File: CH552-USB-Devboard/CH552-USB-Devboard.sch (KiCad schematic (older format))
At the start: 26 parts, among them J1 Conn_01x11_Male, J2 Conn_01x11_Male, J3 USB_C_Receptacle, Q1 CPH6337, SW1 SW_Push, SW2 SW_Push, U1 CH552T, U2 CH552G, U3 MIC5504-3.3YM5, Y1 Crystal

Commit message: add resistors for BOOTL and CC lines, remove LDO
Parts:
- removed C5, C6: 100uF, Capacitor_SMD:C_0603_1608Metric_Pad1.05x0.95mm_HandSolder, symbol Device:C_Small
- removed D4: SMCJ17A+, Diode_SMD:D_1812_4532Metric, symbol Device:D_ALT
- removed JP2: Jumper, Jumper:SolderJumper-2_P1.3mm_Bridged_RoundedPad1.0x1.5mm, symbol Device:Jumper
- removed Q1: CPH6337, TO_SOT_Packages_SMD:SOT-23-6, symbol OnSemi:CPH6337
- removed U3: MIC5504-3.3YM5, Package_TO_SOT_SMD:SOT-23-5, symbol Regulator_Linear:MIC5504-3.3YM5
- removed Y1: Crystal, Crystal:Crystal_SMD_HC49-SD, symbol Device:Crystal
- added D4, D5: e.g. 1N4148, C917006, C708767, Diode_SMD:D_SOD-523, symbol Device:D
- added R1, R2: 68, Resistor_SMD:R_0603_1608Metric_Pad0.98x0.95mm_HandSolder, symbol Device:R_Small
- added R6: 22k, Resistor_SMD:R_0603_1608Metric_Pad0.98x0.95mm_HandSolder, symbol Device:R_Small
- added R7: 220, Resistor_SMD:R_0603_1608Metric_Pad0.98x0.95mm_HandSolder, symbol Device:R_Small
- C3: value 100uF -> 100nF
- C4, C7: value 1uF -> DNP/1uF
- J3: symbol Connector:USB_C_Receptacle -> CH552-USB-Devboard-rescue:USB_C_Receptacle-Connector
- R3, R4: value 330r -> 1k; footprint Resistor_SMD:R_0603_1608Metric_Pad1.05x0.95mm_HandSolder -> Resistor_SMD:R_0603_1608Metric_Pad0.98x0.95mm_HandSolder
- R5: value 300r -> 1k; footprint Resistor_SMD:R_0603_1608Metric_Pad1.05x0.95mm_HandSolder -> Resistor_SMD:R_0603_1608Metric_Pad0.98x0.95mm_HandSolder
- U1: symbol MCU_WCH:CH552T -> CH552-USB-Devboard-rescue:CH552T-MCU_WCH
- U2: symbol MCU_WCH:CH552G -> CH552-USB-Devboard-rescue:CH552G-MCU_WCH
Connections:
- wire segments 161 -> 151
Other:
- note added: "FIXME:\n- BOOTL switch needs 22k resistor\n- RST switch is quite useless (BOOTL needs POR, I think)\n- LDO is not necessary (integrated into the CH552)\n- add solder jumper to bridge Q1\n- add SOT-23 alternative for Q1\n- move crystal to top side?\n- C3 should be 100nF\n- C5/C6 should be *much* smaller, e.g. 12 pF"
- note removed: "Prevents Reverse powering of VBUS"
- note removed: "Reverse Protection\n"
- moved on the sheet: C4

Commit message: add reference voltage for ACMP, replace symbol for USB connector
That symbol was causing warnings because some of the pins are not
available on the footprint. Kicad has the appropriate symbol so
let's use that.
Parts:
- added JP2: Jumper, Jumper:SolderJumper-2_P1.3mm_Bridged_RoundedPad1.0x1.5mm, symbol Jumper:SolderJumper_2_Bridged
- added JP3: Jumper, Jumper:SolderJumper-2_P1.3mm_Open_RoundedPad1.0x1.5mm, symbol Jumper:SolderJumper_2_Open
- added R8: 1k, Resistor_SMD:R_0603_1608Metric_Pad0.98x0.95mm_HandSolder, symbol Device:R_Small
- added R9: 10k, Resistor_SMD:R_0603_1608Metric_Pad0.98x0.95mm_HandSolder, symbol Device:R_Small
- J3: symbol CH552-USB-Devboard-rescue:USB_C_Receptacle-Connector -> Connector:USB_C_Receptacle_USB2.0
- JP1: symbol Device:Jumper -> Jumper:SolderJumper_2_Bridged
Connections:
- net +3V3: now also R9.2
- net GND: now also R8.2
- net P3.2: now also JP2.2 (B), R8.1, R9.1
- net P3.3: now also JP3.2 (B); no longer R7.1
- new net: JP2.1 (A), JP3.1 (A), R7.1
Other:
- note added: "0.5V ref. voltage for ACMP\nOptions:\n1. Both resistors external\n2. Use 10k VBUS pulldown plus ext. PU\n3. Use int. PU plus ext. PD (high variation)\n4. Use int. PU and PD (high variation, 0.5V)"
- note added: "I think P3.2 can do double duty\nbecause we only need the reference\nduring RX and the diode should\nensure that CC1/2 doesn't influence\nthe reference (if Vf>0.5V)."
- note removed: "FIXME:\n- BOOTL switch needs 22k resistor\n- RST switch is quite useless (BOOTL needs POR, I think)\n- LDO is not necessary (integrated into the CH552)\n- add solder jumper to bridge Q1\n- add SOT-23 alternative for Q1\n- move crystal to top side?\n- C3 should be 100nF\n- C5/C6 should be *much* smaller, e.g. 12 pF"
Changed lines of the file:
@@
-	1    0    0    -1
-$EndComp
-$Comp
-L CH552-USB-Devboard-rescue:USB_C_Receptacle-Connector J3
-U 1 1 5F0EEE62
-P 5650 2150
-F 0 "J3" H 5755 3717 50  0000 C CNN
-F 1 "USB_C_Receptacle" H 5755 3626 50  0000 C CNN
-F 2 "footprint:VACON_CSP_USC16_TR" H 5800 2150 50  0001 C CNN
-F 3 "http://www.usb.org/developers/docs/usb_31_033017.zip" H 5800 2150 50  0001 C CNN
-	1    5650 2150
 	1    0    0    -1
 $EndComp
@@
 	6500 1750 6950 1750
 Wire Wire Line
-	5350 3750 5350 4100
-Wire Wire Line
-	5350 4100 5450 4100
-Wire Wire Line
-	5750 3750 5750 4100
-Wire Wire Line
-	5650 3750 5650 4100
-Connection ~ 5650 4100
-Wire Wire Line
-	5650 4100 5750 4100
-Wire Wire Line
-	5550 3750 5550 4100
-Connection ~ 5550 4100
-Wire Wire Line
-	5550 4100 5650 4100
-Wire Wire Line
-	5450 3750 5450 4100
-Connection ~ 5450 4100
-Wire Wire Line
-	5450 4100 5550 4100
-Wire Wire Line
-	5750 4100 5750 4350
-Connection ~ 5750 4100
-$Comp
-L power:GND #PWR0103
-U 1 1 5F12C15E
-P 5750 4350
-F 0 "#PWR0103" H 5750 4100 50  0001 C CNN
-F 1 "GND" H 5755 4177 50  0000 C CNN
-F 2 "" H 5750 4350 50  0001 C CNN
-F 3 "" H 5750 4350 50  0001 C CNN
-	1    5750 4350
-	1    0    0    -1
-$EndComp
-Wire Wire Line
-	6250 850  6750 850
-Wire Wire Line
-	6750 850  6750 700
-Wire Wire Line
-	6250 1150 6750 1150
-Wire Wire Line
-	6750 1150 6750 1050
-Connection ~ 6750 850
-Wire Wire Line
-	6250 1050 6750 1050
-Connection ~ 6750 1050
-Wire Wire Line
-	6750 1050 6750 950
-Wire Wire Line
-	6250 950  6750 950
-Connection ~ 6750 950
-Wire Wire Line
-	6750 950  6750 850
+	6250 1150 6350 1150
 $Comp
 L power:VBUS #PWR0104
 U 1 1 5F1419FC
-P 6750 700
-F 0 "#PWR0104" H 6750 550 50  0001 C CNN
-F 1 "VBUS" H 6765 873 50  0000 C CNN
-F 2 "" H 6750 700 50  0001 C CNN
-F 3 "" H 6750 700 50  0001 C CNN
-	1    6750 700
+P 6350 1050
+F 0 "#PWR0104" H 6350 900 50  0001 C CNN
+F 1 "VBUS" H 6365 1223 50  0000 C CNN
+F 2 "" H 6350 1050 50  0001 C CNN
+F 3 "" H 6350 1050 50  0001 C CNN
+	1    6350 1050
 	1    0    0    -1
 $EndComp
@@
 	1    0    0    -1
 $EndComp
-Text Notes 1250 -650 0    50   ~ 0
-FIXME:\n- BOOTL switch needs 22k resistor\n- RST switch is quite useless (BOOTL needs POR, I think)\n- LDO is not necessary (integrated into the CH552)\n- add solder jumper to bridge Q1\n- add SOT-23 alternative for Q1\n- move crystal to top side?\n- C3 should be 100nF\n- C5/C6 should be *much* smaller, e.g. 12 pF
-$Comp
-L Device:Jumper JP1
+$Comp
+L Jumper:SolderJumper_2_Bridged JP1
 U 1 1 60A07638
 P 8250 1850
 F 0 "JP1" H 8250 2114 50  0000 C CNN
-F 1 "Jumper" H 8250 2023 50  0000 C CNN
+F 1 "Jumper" H 8250 2023 50  0001 C CNN
 F 2 "Jumper:SolderJumper-2_P1.3mm_Bridged_RoundedPad1.0x1.5mm" H 8250 1850 50  0001 C CNN
 F 3 "~" H 8250 1850 50  0001 C CNN
@@
 	1    0    0    -1
 $EndComp
-Wire Wire Line
-	7950 1850 7500 1850
-Wire Wire Line
-	8550 1850 9000 1850
 Wire Wire Line
 	9100 2300 9100 2550
@@
 Wire Wire Line
 	2500 2450 2850 2450
-Text Label 2850 2450 2    50   ~ 0
+Text Label 3650 2700 2    50   ~ 0
 P3.3
 Text Label 800  2300 0    50   ~ 0
@@
 Wire Wire Line
 	9100 4500 9700 4500
+Text Label 2850 2950 2    50   ~ 0
+P3.2
+$Comp
+L Device:R_Small R8
+U 1 1 60A0EBE8
+P 2400 2950
+F 0 "R8" V 2204 2950 50  0000 C CNN
+F 1 "1k" V 2295 2950 50  0000 C CNN
+F 2 "Resistor_SMD:R_0603_1608Metric_Pad0.98x0.95mm_HandSolder" H 2400 2950 50  0001 C CNN
+F 3 "~" H 2400 2950 50  0001 C CNN
+	1    2400 2950
+	0    1    1    0
+$EndComp
+Wire Wire Line
+	2850 2950 2600 2950
+$Comp
+L Device:R_Small R9
+U 1 1 60A17F33
+P 2400 3250
+F 0 "R9" V 2204 3250 50  0000 C CNN
+F 1 "10k" V 2295 3250 50  0000 C CNN
+F 2 "Resistor_SMD:R_0603_1608Metric_Pad0.98x0.95mm_HandSolder" H 2400 3250 50  0001 C CNN
+F 3 "~" H 2400 3250 50  0001 C CNN
+	1    2400 3250
+	0    1    1    0
+$EndComp
+Wire Wire Line
+	2500 3250 2600 3250
+Wire Wire Line
+	2600 3250 2600 2950
+Connection ~ 2600 2950
+Wire Wire Line
+	2600 2950 2500 2950
+$Comp
+L power:+3V3 #PWR0113
+U 1 1 60A21FA3
+P 2200 3250
+F 0 "#PWR0113" H 2200 3100 50  0001 C CNN
+F 1 "+3V3" H 2215 3423 50  0000 C CNN
+F 2 "" H 2200 3250 50  0001 C CNN
+F 3 "" H 2200 3250 50  0001 C CNN
+	1    2200 3250
+	0    -1   -1   0
+$EndComp
+Wire Wire Line
+	2200 3250 2300 3250
+$Comp
+L power:GND #PWR0115
+U 1 1 60A2BA53
+P 2200 2950
+F 0 "#PWR0115" H 2200 2700 50  0001 C CNN
+F 1 "GND" H 2205 2777 50  0000 C CNN
+F 2 "" H 2200 2950 50  0001 C CNN
+F 3 "" H 2200 2950 50  0001 C CNN
+	1    2200 2950
+	0    1    1    0
+$EndComp
+Wire Wire Line
+	2200 2950 2300 2950
+Text Notes 700  3600 0    50   ~ 0
+0.5V ref. voltage for ACMP\nOptions:\n1. Both resistors external\n2. Use 10k VBUS pulldown plus ext. PU\n3. Use int. PU plus ext. PD (high variation)\n4. Use int. PU and PD (high variation, 0.5V)
+$Comp
+L Jumper:SolderJumper_2_Bridged JP2
+U 1 1 60A4E06D
+P 3200 2450
+F 0 "JP2" H 3200 2600 50  0000 C CNN
+F 1 "Jumper" H 3200 2623 50  0001 C CNN
+F 2 "Jumper:SolderJumper-2_P1.3mm_Bridged_RoundedPad1.0x1.5mm" H 3200 2450 50  0001 C CNN
+F 3 "~" H 3200 2450 50  0001 C CNN
+	1    3200 2450
+	1    0    0    -1
+$EndComp
+$Comp
+L Jumper:SolderJumper_2_Open JP3
+U 1 1 60A50BC6
+P 3200 2700
+F 0 "JP3" H 3200 2800 50  0000 C CNN
+F 1 "Jumper" H 3200 2873 50  0001 C CNN
+F 2 "Jumper:SolderJumper-2_P1.3mm_Open_RoundedPad1.0x1.5mm" H 3200 2700 50  0001 C CNN
+F 3 "~" H 3200 2700 50  0001 C CNN
+	1    3200 2700
+	1    0    0    -1
+$EndComp
+Wire Wire Line
+	7500 1850 8100 1850
+Wire Wire Line
+	8400 1850 9000 1850
+Wire Wire Line
+	3650 2700 3350 2700
+Wire Wire Line
+	3050 2700 2850 2700
+Wire Wire Line
+	2850 2700 2850 2450
+Wire Wire Line
+	2850 2450 3050 2450
+Connection ~ 2850 2450
+Text Label 3650 2450 2    50   ~ 0
+P3.2
+Wire Wire Line
+	3650 2450 3350 2450
+Text Notes 2550 2250 0    50   ~ 0
+I think P3.2 can do double duty\nbecause we only need the reference\nduring RX and the diode should\nensure that CC1/2 doesn't influence\nthe reference (if Vf>0.5V).
+$Comp
+L power:GND #PWR0103
+U 1 1 5F12C15E
+P 5650 3250
+F 0 "#PWR0103" H 5650 3000 50  0001 C CNN
+F 1 "GND" H 5655 3077 50  0000 C CNN
+F 2 "" H 5650 3250 50  0001 C CNN
+F 3 "" H 5650 3250 50  0001 C CNN
+	1    5650 3250
+	1    0    0    -1
+$EndComp
+Connection ~ 5650 3000
+Wire Wire Line
+	5650 3000 5650 3250
+Wire Wire Line
+	5350 2650 5350 3000
+Wire Wire Line
+	5650 2650 5650 3000
+$Comp
+L Connector:USB_C_Receptacle_USB2.0 J3
+U 1 1 5F0EEE62
+P 5650 1750
+F 0 "J3" H 5755 3317 50  0000 C CNN
+F 1 "USB_C_Receptacle" H 5755 3226 50  0000 C CNN
+F 2 "footprint:VACON_CSP_USC16_TR" H 5800 1750 50  0001 C CNN
+F 3 "http://www.usb.org/developers/docs/usb_31_033017.zip" H 5800 1750 50  0001 C CNN
+	1    5650 1750
+	1    0    0    -1
+$EndComp
+Wire Wire Line
+	5350 3000 5650 3000
+Wire Wire Line
+	6350 1050 6350 1150
 $EndSCHEMATC

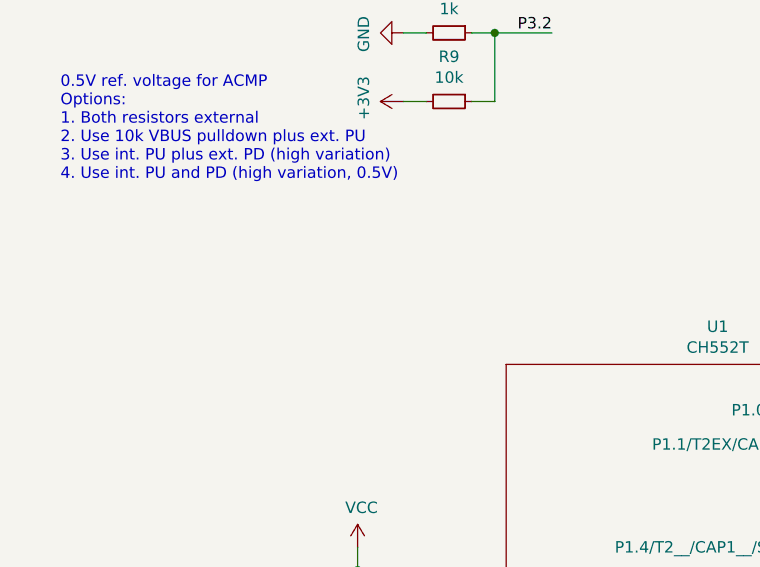
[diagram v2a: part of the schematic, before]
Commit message: add voltage divider for VBUS, optimize GND plane
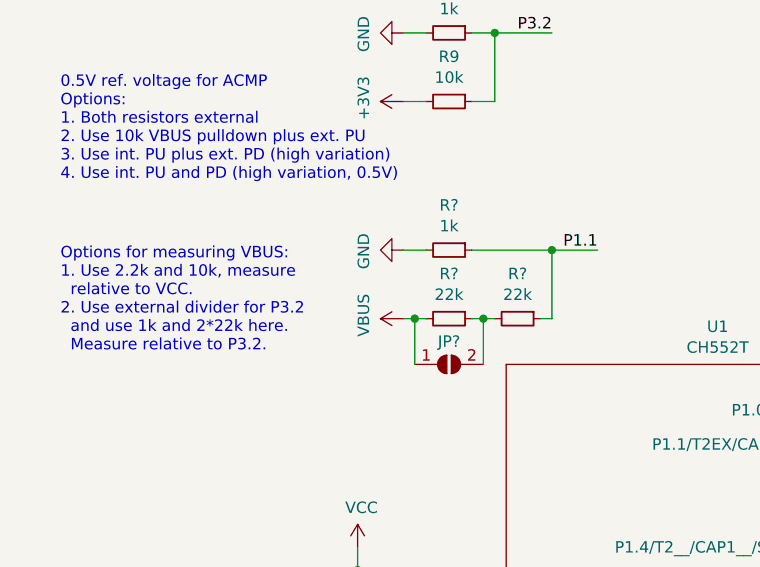
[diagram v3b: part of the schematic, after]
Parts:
- added JP?: Jumper, Jumper:SolderJumper-2_P1.3mm_Open_RoundedPad1.0x1.5mm, symbol Jumper:SolderJumper_2_Open
- added R?: 1k, Resistor_SMD:R_0603_1608Metric_Pad0.98x0.95mm_HandSolder, symbol Device:R_Small
- added R? (x2): 22k, Resistor_SMD:R_0603_1608Metric_Pad0.98x0.95mm_HandSolder, symbol Device:R_Small
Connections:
- net GND: now also R?.2
- net P1.1: now also R?.1, R?.1
- net VBUS: now also JP?.1 (A), R?.2
- new net: JP?.2 (B), R?.1, R?.2
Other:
- note added: "Options for measuring VBUS:\n1. Use 2.2k and 10k, measure\n relative to VCC.\n2. Use external divider for P3.2\n and use 1k and 2*22k here.\n Measure relative to P3.2."
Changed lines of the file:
@@
 Wire Wire Line
 	6350 1050 6350 1150
+Wire Wire Line
+	2850 3900 3050 3900
+Text Label 3050 3900 2    50   ~ 0
+P1.1
+$Comp
+L Device:R_Small R?
+U 1 1 60B6EE8A
+P 2400 3900
+F 0 "R?" V 2204 3900 50  0000 C CNN
+F 1 "1k" V 2295 3900 50  0000 C CNN
+F 2 "Resistor_SMD:R_0603_1608Metric_Pad0.98x0.95mm_HandSolder" H 2400 3900 50  0001 C CNN
+F 3 "~" H 2400 3900 50  0001 C CNN
+	1    2400 3900
+	0    1    1    0
+$EndComp
+$Comp
+L Device:R_Small R?
+U 1 1 60B79ACF
+P 2400 4200
+F 0 "R?" V 2204 4200 50  0000 C CNN
+F 1 "22k" V 2295 4200 50  0000 C CNN
+F 2 "Resistor_SMD:R_0603_1608Metric_Pad0.98x0.95mm_HandSolder" H 2400 4200 50  0001 C CNN
+F 3 "~" H 2400 4200 50  0001 C CNN
+	1    2400 4200
+	0    1    1    0
+$EndComp
+$Comp
+L power:GND #PWR?
+U 1 1 60B79F43
+P 2200 3900
+F 0 "#PWR?" H 2200 3650 50  0001 C CNN
+F 1 "GND" H 2205 3727 50  0000 C CNN
+F 2 "" H 2200 3900 50  0001 C CNN
+F 3 "" H 2200 3900 50  0001 C CNN
+	1    2200 3900
+	0    1    1    0
+$EndComp
+$Comp
+L power:VBUS #PWR?
+U 1 1 60B7AAA5
+P 2200 4200
+F 0 "#PWR?" H 2200 4050 50  0001 C CNN
+F 1 "VBUS" H 2215 4373 50  0000 C CNN
+F 2 "" H 2200 4200 50  0001 C CNN
+F 3 "" H 2200 4200 50  0001 C CNN
+	1    2200 4200
+	0    -1   -1   0
+$EndComp
+Wire Wire Line
+	2200 4200 2250 4200
+Wire Wire Line
+	2300 3900 2200 3900
+Wire Wire Line
+	2850 4200 2850 3900
+Connection ~ 2850 3900
+Text Notes 700  4350 0    50   ~ 0
+Options for measuring VBUS:\n1. Use 2.2k and 10k, measure\n  relative to VCC.\n2. Use external divider for P3.2\n  and use 1k and 2*22k here.\n  Measure relative to P3.2.
+$Comp
+L Device:R_Small R?
+U 1 1 60BB508E
+P 2700 4200
+F 0 "R?" V 2504 4200 50  0000 C CNN
+F 1 "22k" V 2595 4200 50  0000 C CNN
+F 2 "Resistor_SMD:R_0603_1608Metric_Pad0.98x0.95mm_HandSolder" H 2700 4200 50  0001 C CNN
+F 3 "~" H 2700 4200 50  0001 C CNN
+	1    2700 4200
+	0    1    1    0
+$EndComp
+Wire Wire Line
+	2500 3900 2850 3900
+$Comp
+L Jumper:SolderJumper_2_Open JP?
+U 1 1 60BC9416
+P 2400 4400
+F 0 "JP?" H 2400 4500 50  0000 C CNN
+F 1 "Jumper" H 2400 4573 50  0001 C CNN
+F 2 "Jumper:SolderJumper-2_P1.3mm_Open_RoundedPad1.0x1.5mm" H 2400 4400 50  0001 C CNN
+F 3 "~" H 2400 4400 50  0001 C CNN
+	1    2400 4400
+	1    0    0    -1
+$EndComp
+Wire Wire Line
+	2800 4200 2850 4200
+Wire Wire Line
+	2550 4400 2550 4200
+Wire Wire Line
+	2550 4200 2500 4200
+Wire Wire Line
+	2550 4200 2600 4200
+Connection ~ 2550 4200
+Wire Wire Line
+	2250 4400 2250 4200
+Connection ~ 2250 4200
+Wire Wire Line
+	2250 4200 2300 4200
 $EndSCHEMATC
